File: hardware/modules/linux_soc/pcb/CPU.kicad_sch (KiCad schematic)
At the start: 17 parts, among them U1 F1C100s

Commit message: Got further with linux soc module
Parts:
- added J2: USB_C_Receptacle_USB2.0_16P, symbol Connector:USB_C_Receptacle_USB2.0_16P
- added R5, R6: 5k1, symbol Device:R
- added R7, R8: 22R, symbol Device:R
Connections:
- net GND: now also J2.A1 (GND), J2.A12 (GND), J2.B1 (GND), J2.B12 (GND), J2.SH (SHIELD), R5.2, R6.2
- net at U1.68 (USB-DM): now also R7.1
- net at U1.69 (USB-DP): now also R8.1
- new net: J2.A5 (CC1), R5.1
- new net: J2.B5 (CC2), R6.1
- new net +5V: J2.A4 (VBUS), J2.A9 (VBUS), J2.B4 (VBUS), J2.B9 (VBUS)
- new net USB-DM: J2.A7 (D-), J2.B7 (D-), R7.2
- new net USB-DP: J2.A6 (D+), J2.B6 (D+), R8.2
- no-connect marks 3 -> 5
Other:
- moved on the sheet: C10, C11, C12, C13, C14, C15, C16, C17, C18, C19, C20, C21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

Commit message: Added Crystal and SD card to linux soc card
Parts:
- added C23, C24: C, symbol Device:C
- added Y1: 24MHz, symbol Device:Crystal_GND24
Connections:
- net GND: now also C23.2, C24.2, Y1.2 (G), Y1.4 (G)
- net HOSCI: now reaches U1.51 (HOSCI)
- net HOSCI: now also C23.1, Y1.3
- net HOSCO: now reaches U1.52 (HOSCO)
- net HOSCO: now also C24.1, Y1.1
- net DAT2: now reaches U1.53 (PF5)
- net DAT3: now reaches U1.54 (PF4)
- net CMD: now reaches U1.55 (PF3)
- net CLK: now reaches U1.56 (PF2)
- net DAT0: now reaches U1.57 (PF1)
- net DAT1: now reaches U1.58 (PF0)

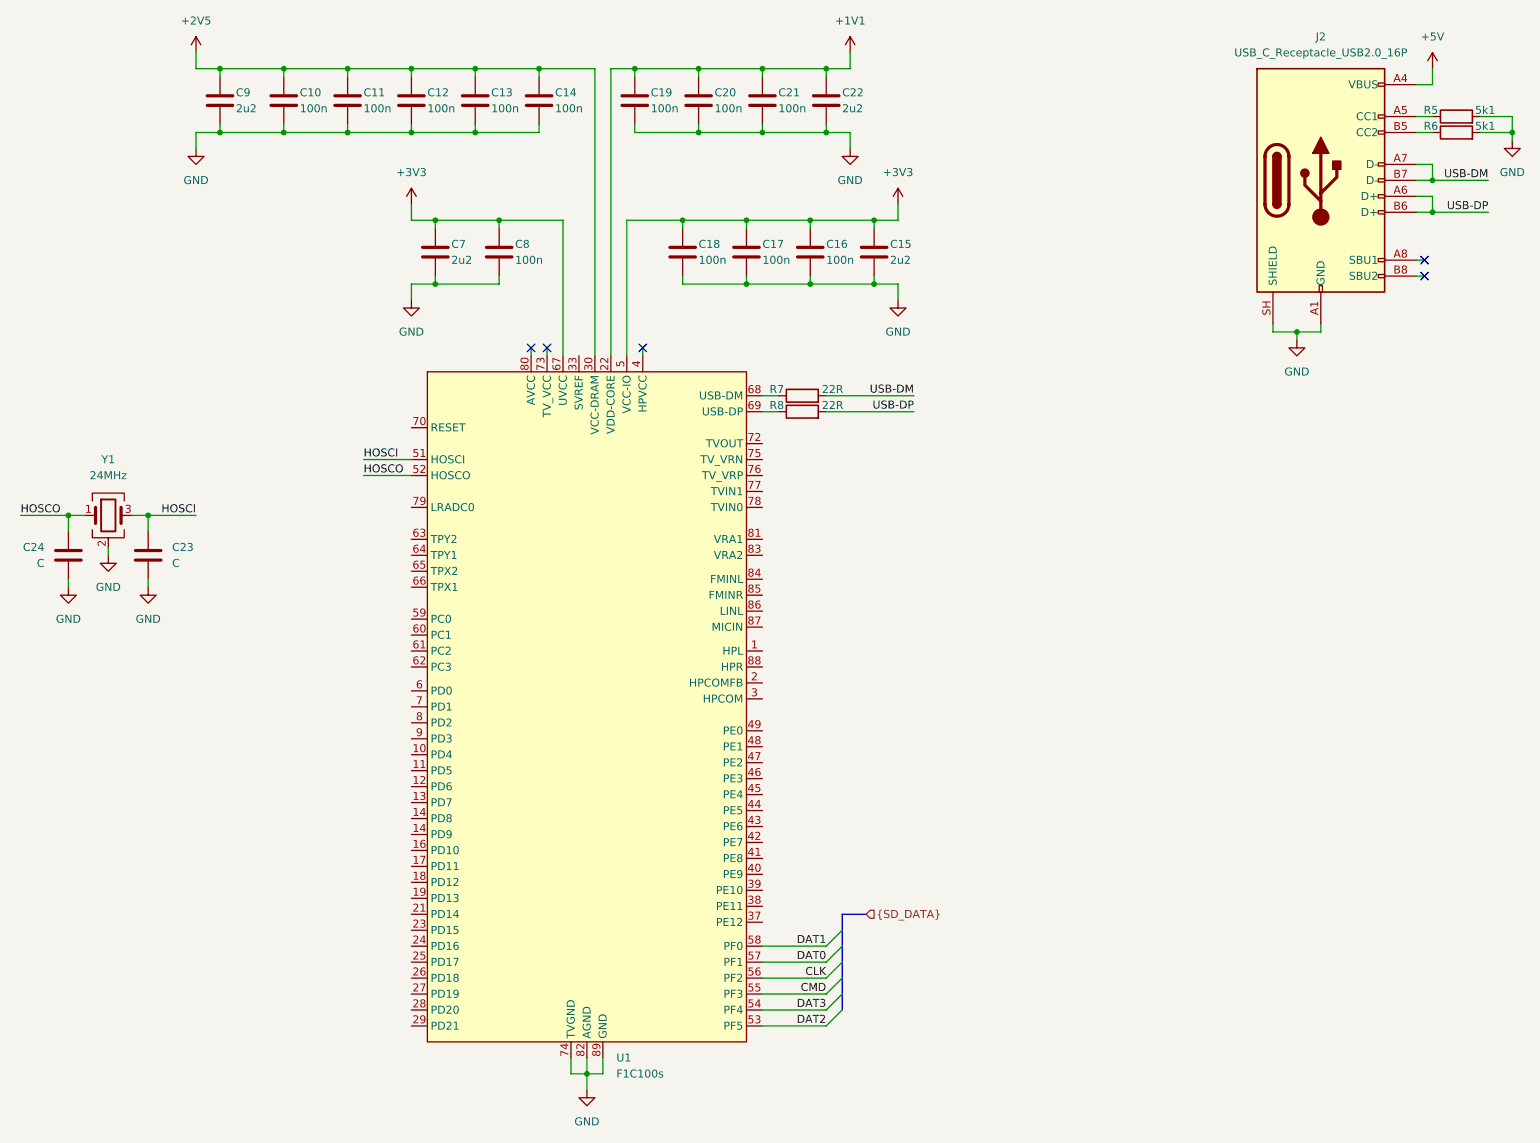
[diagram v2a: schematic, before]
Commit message: Started on PCB layout finished schematic
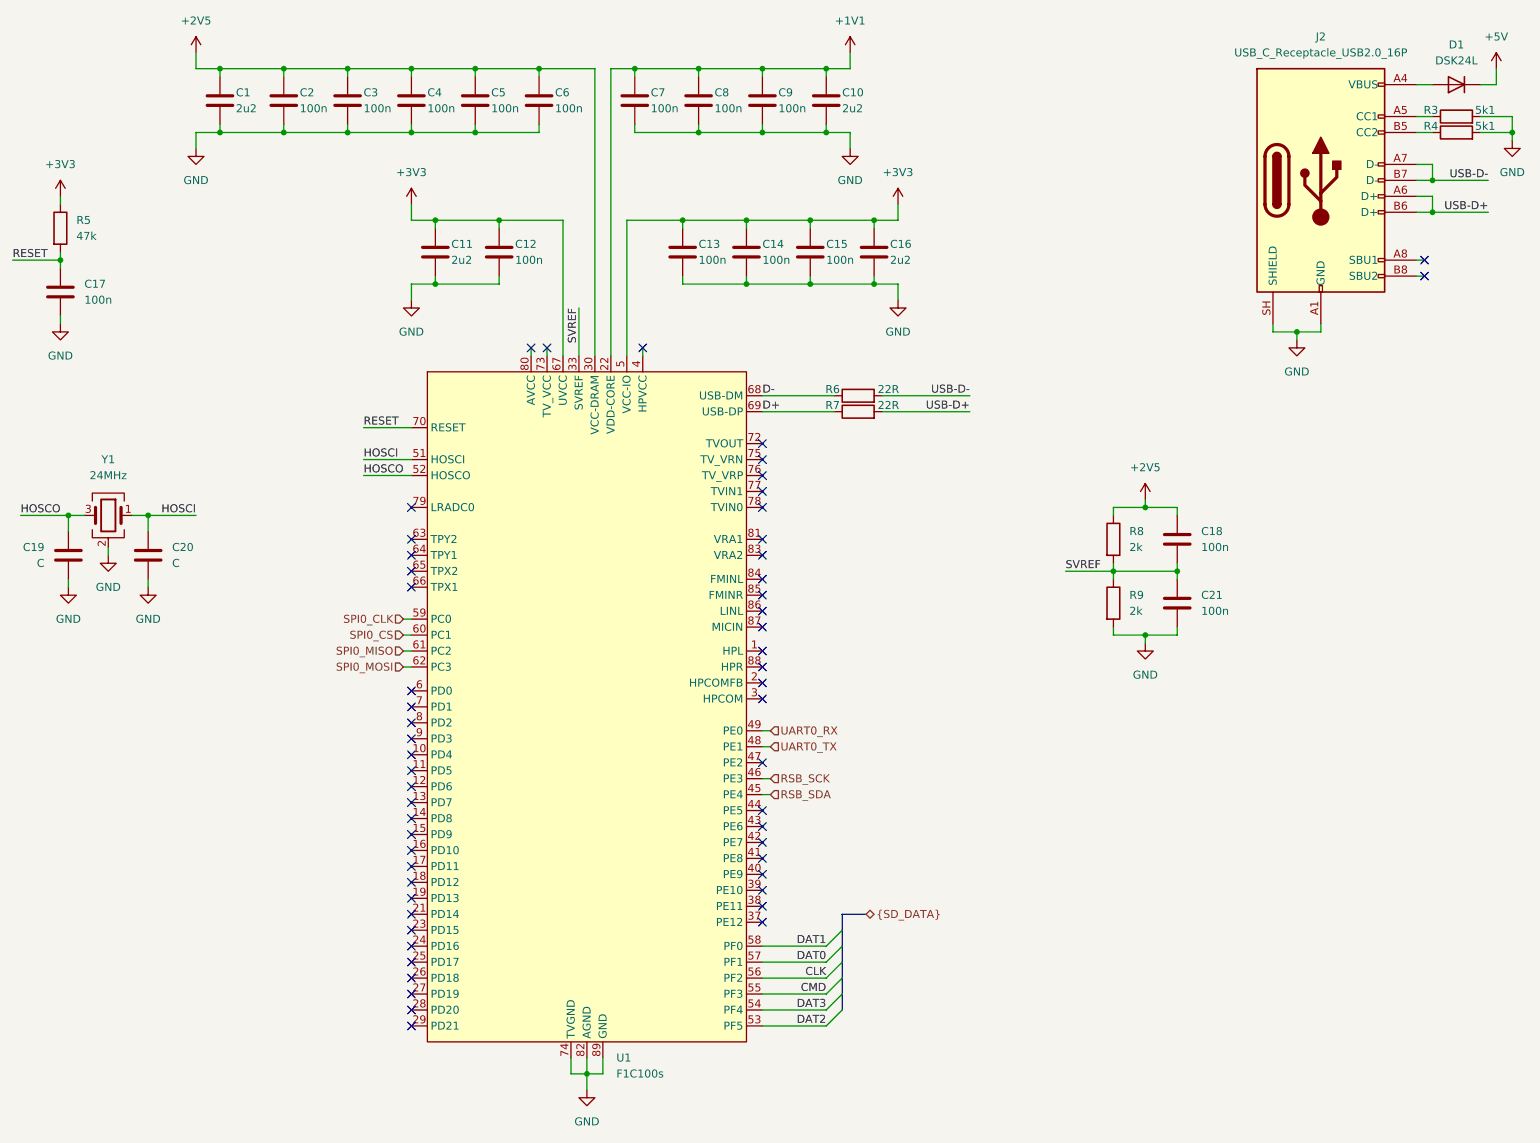
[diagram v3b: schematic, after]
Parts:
- added C17, C18, C21: 100n, Capacitor_SMD:C_0402_1005Metric, symbol Device:C
- added D1: DSK24L, Diode_SMD:D_SOD-123F, symbol Device:D
- added R5: 47k, Resistor_SMD:R_0402_1005Metric, symbol Device:R
- added R8, R9: 2k, Resistor_SMD:R_0402_1005Metric, symbol Device:R
- C1: renamed from C9; footprint (none) -> Capacitor_SMD:C_0402_1005Metric
- C10: renamed from C22; footprint (none) -> Capacitor_SMD:C_0402_1005Metric
- C11: renamed from C7; footprint (none) -> Capacitor_SMD:C_0402_1005Metric
- C12: renamed from C8; footprint (none) -> Capacitor_SMD:C_0402_1005Metric
- C13: renamed from C18; footprint (none) -> Capacitor_SMD:C_0402_1005Metric
- C14: renamed from C17; footprint (none) -> Capacitor_SMD:C_0402_1005Metric
- C15: renamed from C16; footprint (none) -> Capacitor_SMD:C_0402_1005Metric
- C16: renamed from C15; footprint (none) -> Capacitor_SMD:C_0402_1005Metric
- C19: renamed from C24; footprint (none) -> Capacitor_SMD:C_0402_1005Metric
- C2: renamed from C10; footprint (none) -> Capacitor_SMD:C_0402_1005Metric
- C20: renamed from C23; footprint (none) -> Capacitor_SMD:C_0402_1005Metric
- C3: renamed from C11; footprint (none) -> Capacitor_SMD:C_0402_1005Metric
- C4: renamed from C12; footprint (none) -> Capacitor_SMD:C_0402_1005Metric
- C5: renamed from C13; footprint (none) -> Capacitor_SMD:C_0402_1005Metric
- C6: renamed from C14; footprint (none) -> Capacitor_SMD:C_0402_1005Metric
- C7: renamed from C19; footprint (none) -> Capacitor_SMD:C_0402_1005Metric
- C8: renamed from C20; footprint (none) -> Capacitor_SMD:C_0402_1005Metric
- C9: renamed from C21; footprint (none) -> Capacitor_SMD:C_0402_1005Metric
- J2: footprint (none) -> Connector_USB:USB_C_Receptacle_GCT_USB4105-xx-A_16P_TopMnt_Horizontal; LCSC# (none) -> C165948
- R3: renamed from R5; footprint (none) -> Resistor_SMD:R_0402_1005Metric
- R4: renamed from R6; footprint (none) -> Resistor_SMD:R_0402_1005Metric
- R6: renamed from R7; footprint (none) -> Resistor_SMD:R_0402_1005Metric
- R7: renamed from R8; footprint (none) -> Resistor_SMD:R_0402_1005Metric
- U1: LCSC# (none) -> C1511928
- Y1: footprint (none) -> Crystal:Crystal_SMD_2016-4Pin_2.0x1.6mm
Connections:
- net +2V5: now also C18.1, R8.1
- net +3V3: now also R5.1
- net +5V: now also D1.1 (K); no longer J2.A4 (VBUS), J2.A9 (VBUS), J2.B4 (VBUS), J2.B9 (VBUS)
- net GND: now also C17.2, C21.2, R9.2
- net HOSCI: now also Y1.1; no longer Y1.3
- net HOSCO: now also Y1.3; no longer Y1.1
- net D+: now reaches R7.1, U1.69 (USB-DP)
- net SVREF: now reaches U1.33 (SVREF)
- net SVREF: now also C18.2, C21.1, R8.2, R9.1
- net RSB_SDA: now reaches U1.45 (PE4)
- net RSB_SCK: now reaches U1.46 (PE3)
- net UART0_TX: now reaches U1.48 (PE1)
- net UART0_RX: now reaches U1.49 (PE0)
- net SPI0_CLK: now reaches U1.59 (PC0)
- net SPI0_CS: now reaches U1.60 (PC1)
- net SPI0_MISO: now reaches U1.61 (PC2)
- net SPI0_MOSI: now reaches U1.62 (PC3)
- net D-: now reaches R6.1, U1.68 (USB-DM)
- net RESET: now reaches U1.70 (RESET)
- net RESET: now also C17.1, R5.2
- net USB-DM renamed USB-D-
- net USB-DP renamed USB-D+
- new net: D1.2 (A), J2.A4 (VBUS), J2.A9 (VBUS), J2.B4 (VBUS), J2.B9 (VBUS)
- no-connect marks 5 -> 56
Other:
- moved on the sheet: R6, R7
